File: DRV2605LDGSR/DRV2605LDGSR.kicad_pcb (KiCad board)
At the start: 2 copper layers, 15.2 x 15.2 mm, 3 parts, among them J1 Conn_01x05_Female, J2 Conn_01x05_Female, U1 DRV2605LDGSR

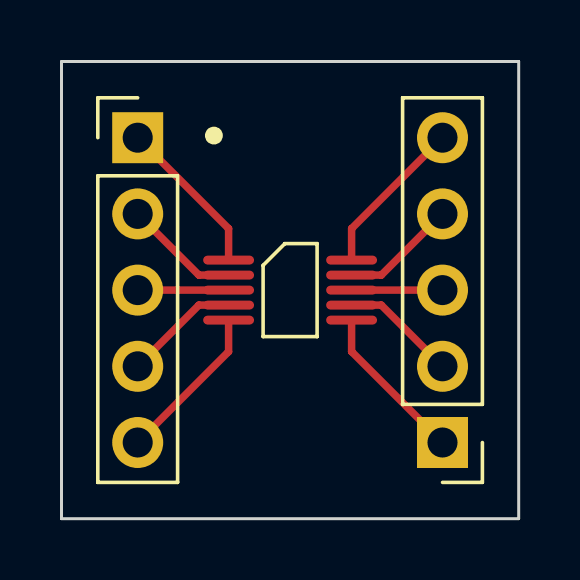
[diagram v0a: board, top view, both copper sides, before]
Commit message: New breakout started, ADS1219, because th ADS112C04 is out of stock everywhere
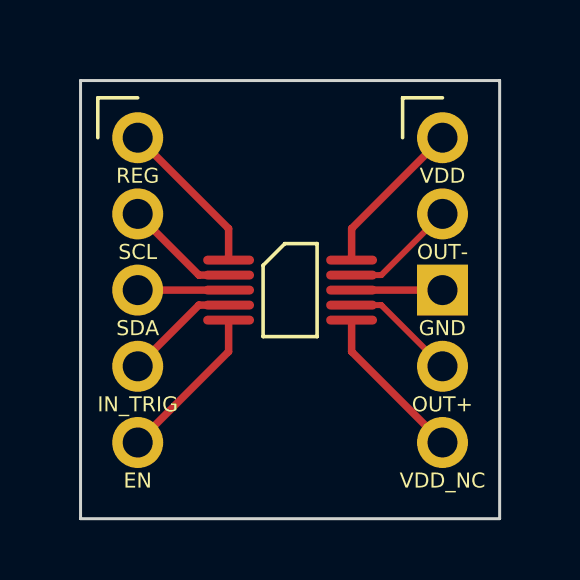
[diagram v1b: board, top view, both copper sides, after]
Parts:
- J1, J2: value Conn_01x05_Female -> Conn_01x05
- moved J2 10.2 mm to (154.9, 58.4), turned to 0 degrees
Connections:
- net Net-(U1-Pad1) renamed /REG
- net Net-(U1-Pad2) renamed /SCL
- net Net-(U1-Pad3) renamed /SDA
- net Net-(U1-Pad4) renamed /IN_TRIG
- net Net-(U1-Pad5) renamed /EN
- net Net-(U1-Pad8) renamed GND
- J2 pad 1: Net-(U1-Pad6) -> /VDD
- J2 pad 2: Net-(U1-Pad7) -> /OUT-
- J2 pad 4: Net-(U1-Pad9) -> /OUT+
- J2 pad 5: Net-(U1-Pad10) -> /VDD_NC
- U1 pad 10: Net-(U1-Pad10) -> /VDD
- U1 pad 6: Net-(U1-Pad6) -> /VDD_NC
- U1 pad 7: Net-(U1-Pad7) -> /OUT+
- U1 pad 9: Net-(U1-Pad9) -> /OUT-
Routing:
- net Net-(U1-Pad10): track 5.34 -> 0.00 mm
- net /VDD: track 0.00 -> 5.34 mm
- net Net-(U1-Pad6): track 5.34 -> 0.00 mm
- net /VDD_NC: track 0.00 -> 5.34 mm
- net Net-(U1-Pad7): track 3.87 -> 0.00 mm
- net /OUT+: track 0.00 -> 3.87 mm
- net Net-(U1-Pad9): track 3.87 -> 0.00 mm
- net /OUT-: track 0.00 -> 3.87 mm
- added copper zone on B.Cu, net GND
- added copper zone on F.Cu, net GND
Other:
- board size 15.2 x 15.2 mm -> 14 x 14.6 mm
- board text added: "EN"
- board text added: "GND"
- board text added: "IN_TRIG"
- board text added: "OUT+"
- board text added: "OUT-"
- board text added: "REG"
- board text added: "SCL"
- board text added: "SDA"
- board text added: "VDD"
- board text added: "VDD_NC"
- board text removed: "•"
